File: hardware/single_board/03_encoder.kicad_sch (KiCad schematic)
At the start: 2 parts, among them U10 MT6701

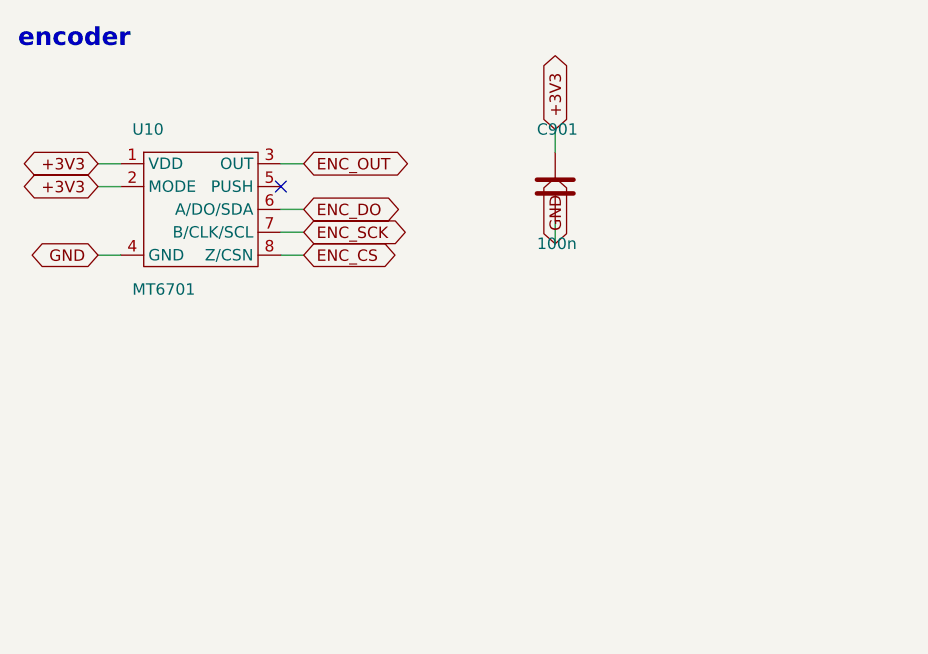
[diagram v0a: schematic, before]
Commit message: Board S schematic: drawn as a person would draw it
The sheets were a grid of parts with a stub and a label on every pin.
tools/schdraw.py now draws a netlist from a hand-written layout: parts
placed and turned, wires between the pins that belong together, T-joins
split with a junction dot, ground and supply symbols on power pins, labels
only where a signal leaves its block. tools/schlayout_s.py is board S's
five sheets: signal left to right, supplies up, ground down, each part's
support parts at the pin they serve, dashed frames and notes.

The drawing cannot change the circuit: every sheet is checked against
schematic_s's netlist before it is written, and `schdraw.py --check s`
compares KiCad's own netlist export net by net (it matches; ERC 0 at all
severities; PCB parity unchanged, same 219 reports as before).

Found on the way: a symbol's instance path must be /<root>/<sheet>. With
the root left out, as schematic.py writes it, KiCad joins labelled nets
but silently drops every net that is only wire.

Co-Authored-By: Claude Opus 5.5 (1M context) <noreply@anthropic.com>
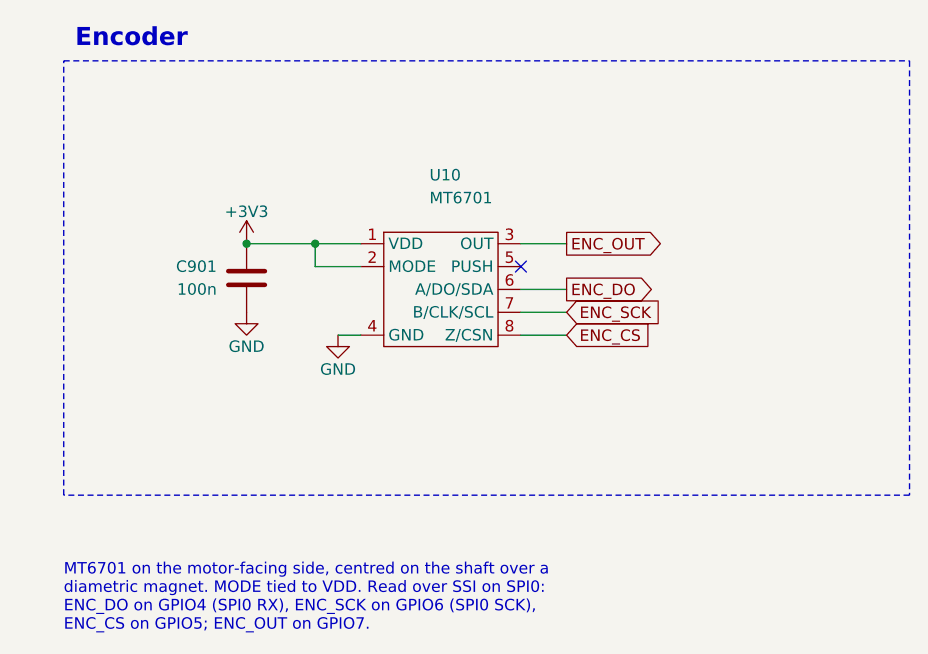
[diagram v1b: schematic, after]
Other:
- note added: "Encoder"
- note added: "MT6701 on the motor-facing side, centred on the shaft over a diametric magnet. MODE tied to VDD. Read over SSI on SPI0: ENC_DO on GPIO4 (SPI0 RX), ENC_SCK on GPIO6 (SPI0 SCK), ENC_CS on GPIO5; ENC_OUT on GPIO7."
- note removed: "encoder"
- moved on the sheet: C901, U10

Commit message: Board S schematic: the header and the notes follow the netlist
J13's pins are drawn by net (VBUS row, ground row, supply pins on staggered
stubs, labels for the rest), and the encoder note reads its GPIOs off U7, so
the same layout draws main's pin map and this branch's.

Co-Authored-By: Claude Opus 5.5 (1M context) <noreply@anthropic.com>
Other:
- note added: "MT6701 on the motor-facing side, centred on the shaft over a diametric magnet. MODE tied to VDD. The CPU reads it over SSI (sheet 02)."
- note removed: "MT6701 on the motor-facing side, centred on the shaft over a diametric magnet. MODE tied to VDD. Read over SSI on SPI0: ENC_DO on GPIO4 (SPI0 RX), ENC_SCK on GPIO6 (SPI0 SCK), ENC_CS on GPIO5; ENC_OUT on GPIO7."
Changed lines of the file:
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@@
 		(effects (font (size 2.0 2.0) (bold yes)) (justify left bottom))
 )
-	(text "MT6701 on the motor-facing side, centred on the shaft over a\ndiametric magnet. MODE tied to VDD. Read over SSI on SPI0:\nENC_DO on GPIO4 (SPI0 RX), ENC_SCK on GPIO6 (SPI0 SCK),\nENC_CS on GPIO5; ENC_OUT on GPIO7." (exclude_from_sim no)
+	(text "MT6701 on the motor-facing side, centred on the shaft over a\ndiametric magnet. MODE tied to VDD. The CPU reads it over\nSSI (sheet 02)." (exclude_from_sim no)
 		(at 20.3200 80.0100 0)
 		(effects (font (size 1.27 1.27)) (justify left top))
